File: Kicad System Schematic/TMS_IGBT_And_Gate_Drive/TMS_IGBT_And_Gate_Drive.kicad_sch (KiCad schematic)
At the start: 45 parts, among them J1 AFBR-1624Z, J2 AFBR-1624Z, J3 AFBR-2624Z, J4 AFBR-2624Z, J5 AFBR-2624Z, J6 AFBR-1624Z, J7 AFBR-2624Z, J8 AFBR-1624Z, Q1 FZ1200R33KF2, Q2 FZ1200R33KF2, T1 Microwave-Oven Transformer, T2 Microwave-Oven Transformer, T3 Variable Transformer, U1 Isolated DC-DC Converter, U2 Non-Isolated DC-DC Converter, U5 1SD418F2-FZ1200R33KF2, U6 1SD418F2-FZ1200R33KF2, U7 74HCT125N, U8 Non-Isolated DC-DC Converter

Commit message: updated schematic with some untested charge-controller circuitry. This is something I plan on building and testing.
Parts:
- added C17, C18, C22, C24: 100n, symbol Device:C
- added C19, C20, C21, C23, C27, C29, C33: 10u, symbol Device:C
- added C25, C30, C32: 1u, symbol Device:C
- added C26, C31: 0.1u, symbol Device:C
- added C28: 10000p, symbol Device:C
- added R1, R2: 4k7, symbol Device:R
- added R10, R11, R6, R9: 0, symbol Device:R
- added R12, R13, R14, R3, R4, R5: 5k1, symbol Device:R
- added R15, R16, R17, R18, R19, R20, R21, R22: 1M, Resistor_SMD:R_2512_6332Metric_Pad1.40x3.35mm_HandSolder, symbol Device:R
- added R7, R8: 10K, Resistor_SMD:R_1206_3216Metric_Pad1.30x1.75mm_HandSolder, symbol Device:R
- added U11: LM2931-5.0_SO8, Package_SO:SOIC-8_3.9x4.9mm_P1.27mm, symbol Regulator_Linear:LM2931-5.0_SO8
- added U12: ADS1115IDGS, Package_SO:TSSOP-10_3x3mm_P0.5mm, symbol Analog_ADC:ADS1115IDGS
- added U3: LM393, symbol Comparator:LM393
- added U4: AD5693RxRM, Package_SO:MSOP-10_3x3mm_P0.5mm, symbol Analog_DAC:AD5693RxRM
- added U9: Non-Isolated DC-DC Converter, Converter_DCDC:Converter_DCDC_Murata_OKI-78SR_Horizontal, symbol Converter_DCDC:OKI-78SR-5_1.5-W36H-C
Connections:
- net +24V: now also U9.1 (IN)
- net +3V3: now also C32.2, C33.2, U4.2 (VLOGIC)
- net +5V: now also C17.1, C18.1, C19.1, C20.1, C21.1, C22.1, C23.1, C24.1
- net GND: now also C1.2, C10.2, C11.2, C12.2, C13.2, C14.2, C15.2, C16.2, C2.2, D2.2 (A), D5.2 (A), D6.2 (A), MES2.2 (-), Q2.4 (Emitter_phase_1), Q2.6 (Emitter_phase_2), Q2.8 (Emitter_phase_3), C17.2, C18.2, C19.2, C20.2, C21.2, C22.2, C23.2, C24.2, C25.2, C26.2, C27.2, C28.2, C29.2, C30.2, C31.2, C32.1, C33.1, R1.1, R11.2, R2.1, R7.1, R8.1, R9.2, U11.2 (GND), U11.3 (GND), U11.6 (GND), U11.7 (GND), U12.3 (GND), U12.5 (AIN1), U12.6 (AIN2), U12.7 (AIN3), U12.8 (VDD), U4.4 (~{LDAC}), U4.5 (GND), U9.2 (GND)
- net at C1.1, C2.1, C3.1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: now also R15.2, R22.2
- new net: J1.4 (Fiber_Out), J2.4 (Fiber_Out), R1.2, R2.2, U7.3 (1Y)
- new net: R10.2, R11.1, U12.1 (ADDR)
- new net: R15.1, R16.2
- new net: R5.2, U4.3 (~{RESET})
- new net: R17.1, R18.2
- new net: R16.1, R17.2
- new net: R19.2, R20.1
- new net: R20.2, R21.1
- new net: R19.1, R7.2, U3.3 (+)
- new net: C28.1, U4.9 (VREF)
- new net: R18.1, R8.2, U12.4 (AIN0)
- new net: R21.2, R22.1
- new net: U3.2 (-), U4.10 (VOUT)
- new net: R6.2, R9.1, U4.6 (A0)
- new net +5V_LDO: C25.1, C26.1, C27.1, C29.1, C30.1, C31.1, R10.1, R12.1, R13.1, R14.1, R3.1, R4.1, R5.1, R6.1, U11.1 (OUT), U4.1 (VDD)
- new net +8V: U11.8 (IN), U9.3 (OUT)
- new net ADC_INT: R12.2, U12.2 (ALERT/RDY)
- new net ADC_SCL: R13.2, U12.10 (SCL)
- new net ADC_SDA: R14.2, U12.9 (SDA)
- new net DAC_SCL: R3.2, U4.7 (SCL)
- new net DAC_SDA: R4.2, U4.8 (SDA)
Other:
- note added: "COMPARATOR"
- note added: "DAC"
- note added: "HV Voltage Divider 1"
- note added: "HV Voltage Divider 2"

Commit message: updated schematic. Tried using DAC and comparator, it's too noisey, can't use opamps to filter noise. Instead using dedicated teensy to read ADC, do digital filtering/averaging and control charge circuit
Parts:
- added C34: 4u7, symbol Device:C
- added C35, C37: 1u, symbol Device:C
- added C36, C38, C39, C40: 10u, symbol Device:C
- added Q3: IRG4PF50W, Package_TO_SOT_THT:TO-247-3_Vertical, symbol Transistor_IGBT:IRG4PF50W
- added R23: 10, symbol Device:R
- added U10: MCP1415, Package_TO_SOT_SMD:SOT-23-5, symbol Driver_FET:MCP1415
- added U13: Isolated DC-DC Converter, Converter_DCDC:Converter_DCDC_Artesyn_ATA_SMD, symbol Converter_DCDC_Isolated:ATA00A36S-L
- added U14: ISO1644DWR, Package_SO:SOIC-16W_7.5x10.3mm_P1.27mm, symbol Isolator:ISO1644DWR
- added U15: LM2931-5.0_SO8, Package_SO:SOIC-8_3.9x4.9mm_P1.27mm, symbol Regulator_Linear:LM2931-5.0_SO8
- added U16: ADS8699IPWR, symbol Analog_ADC:ADS8699IPWR
- C28: footprint (none) -> Capacitor_SMD:C_0603_1608Metric
- U4: footprint Package_SO:MSOP-10_3x3mm_P0.5mm -> AD5683RARMZ:AD5683RARMZ
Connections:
- net +24V: now also U13.16 (+VIN)
- net +3V3: now also C40.1, U14.1 (VCC1)
- net DAC_SCL: now also A1.19 (I2C_0_SCL)
- net DAC_SDA: now also A1.18 (I2C_0_SDA)
- net GND: now also C40.2, Q3.2 (C), U13.1 (-VIN), U14.2 (GND1), U14.8 (GND1); no longer D5.2 (A), D6.2 (A), R8.1
- net ISO_+15V: now also U10.2 (Vdd)
- net ISO_GND: now also R8.1, C34.2, C35.2, C36.2, C37.2, C38.2, C39.2, U10.4 (GND), U13.10 (-VOUT), U14.15 (GND2), U14.9 (GND2), U15.2 (GND), U15.3 (GND), U15.6 (GND), U15.7 (GND), U16.1 (AGND), U16.15 (DGND), U16.3 (REFGND), U16.6 (AIN_GND)
- net at R18.1, R8.2, U12.4 (AIN0): now also U16.5 (AIN_P)
- net Charge_Switch: now reaches U3.1
- net Charge_Switch: now also U10.3 (IN)
- new net: U14.10 (INC), U16.11 (SDO-0)
- new net: U14.11 (SCL2), U16.7 (~{RST})
- new net: U14.12 (OUTB), U16.8 (SDI)
- new net: U14.13 (OUTA), U16.10 (SCLK)
- new net: U14.14 (SDA2), U16.9 (CONVST/~{CS})
- new net: Q3.1 (G), R23.1
- new net: D5.2 (A), D6.2 (A), Q3.3 (E)
- new net: C35.1, C36.1, U16.4 (REFCAP)
- new net: C34.1, U16.2 (REFIO)
- new net: R23.2, U10.5 (~{OUT})
- new net ISO_+5V_LDO: C37.1, C38.1, C39.1, U14.16 (VCC2), U15.1 (OUT), U16.14 (DVDD), U16.16 (AVDD)
- new net ISO_+8V: U13.9 (+VOUT), U15.8 (IN)
- new net ISO_ADC_CS/CONVST: A1.10 (SPI_0_CS), U14.3 (SDA1)
- new net ISO_ADC_RST: A1.9 (Digital_Out), U14.6 (SCL1)
- new net ISO_ADC_SCLK: A1.13 (SPI_0_SCK), U14.4 (INA)
- new net ISO_ADC_SDI: A1.11 (SPI_0_MOSI), U14.7 (OUT)
- new net ISO_ADC_SDO: A1.12 (SPI_0_MISO), U14.5 (INB)
- no-connect marks 7 -> 8
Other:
- note added: "PROBABLY NOT GOING TO USE DAC AND COMPARATOR. Can't find a way to filter noise in divided voltage. easier to filter/average digitally in teensy."
- note added: "PROBABLY NOT GOING TO USE THIS ADC. Using the ADS8699IPWR instead for higher sample rate"
- note added: "To Teensy"
- moved on the sheet: C25, C26, C27, C28, C29, C30, C31, C32, C33, D1, D4, D5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

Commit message: started updating schematic, need to find better symbol for the high voltage differential probes... Added first-draft of Bill-Of-Materials, just got the main power components for now. Will next add all components for the charge-controller and pulse-driver. Still need to upgrade pulse-driver to handle different protocols & patterns and have a single-shot mode. Right now I'm excited about finally building a system to measure/characterize and map the magnetic field strength of various coils I made compared to the one commercial coil I have. Can then compare these results to the simulations.
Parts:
- removed C39, C40: 10u, symbol Device:C
- removed R15, R16, R17, R18, R19, R20, R21, R22: 1M, Resistor_SMD:R_2512_6332Metric_Pad1.40x3.35mm_HandSolder, symbol Device:R
- removed R7, R8: 10K, Resistor_SMD:R_1206_3216Metric_Pad1.30x1.75mm_HandSolder, symbol Device:R
- removed U13: Isolated DC-DC Converter, Converter_DCDC:Converter_DCDC_Artesyn_ATA_SMD, symbol Converter_DCDC_Isolated:ATA00A36S-L
- removed U14: ISO1644DWR, Package_SO:SOIC-16W_7.5x10.3mm_P1.27mm, symbol Isolator:ISO1644DWR
- removed U15: LM2931-5.0_SO8, Package_SO:SOIC-8_3.9x4.9mm_P1.27mm, symbol Regulator_Linear:LM2931-5.0_SO8
- added MES4: HV Differential Probe, symbol Simulation_SPICE:VOLTMETER_DIFF
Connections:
- net ISO_+5V_LDO is gone; now on net +5V_LDO: C37.1, C38.1, U16.14 (DVDD), U16.16 (AVDD)
- net ISO_ADC_CS/CONVST is gone; now on net ADC_CS/CONVST: A1.10 (SPI_0_CS)
- net ISO_ADC_RST is gone; now on net ADC_RST: A1.9 (Digital_Out)
- net ISO_ADC_SCLK is gone; now on net ADC_SCLK: A1.13 (SPI_0_SCK)
- net ISO_ADC_SDI is gone; now on net ADC_SDI: A1.11 (SPI_0_MOSI)
- net ISO_ADC_SDO is gone; now on net ADC_SDO: A1.12 (SPI_0_MISO)
- net GND: now also C34.2, C35.2, C36.2, C37.2, C38.2, U16.1 (AGND), U16.15 (DGND), U16.3 (REFGND), U16.6 (AIN_GND), MES4.2 (-)
- net ISO_GND: no longer C34.2, C35.2, C36.2, C37.2, C38.2, U16.1 (AGND), U16.15 (DGND), U16.3 (REFGND), U16.6 (AIN_GND)
- net at C1.1, C2.1, C3.1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: now also MES4.1 (+)
- net ADC_SDO: now reaches U16.11 (SDO-0)
- net ADC_RST: now reaches U16.7 (~{RST})
- net ADC_SDI: now reaches U16.8 (SDI)
- net ADC_SCLK: now reaches U16.10 (SCLK)
- net ADC_CS/CONVST: now reaches U16.9 (CONVST/~{CS})
- net at U3.3 (+): now also U12.4 (AIN0), U16.5 (AIN_P), MES4.3 (out)
- net ADC_RVS: now reaches U16.13 (RVS)
- net ADC_RVS: now also A1.6 (Digital_In)
- net +8V renamed +7V5
- no-connect marks 8 -> 7
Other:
- note added: "Keeping this slow speed ADC to be able to verify the DAC output, and verify the high-speed ADC"
- note removed: "HV Voltage Divider 1"
- note removed: "HV Voltage Divider 2"
- note removed: "PROBABLY NOT GOING TO USE DAC AND COMPARATOR. Can't find a way to filter noise in divided voltage. easier to filter/average digitally in teensy."
- note removed: "PROBABLY NOT GOING TO USE THIS ADC. Using the ADS8699IPWR instead for higher sample rate"
- moved on the sheet: C25, C26, C27, C28, C32, C33, R3, R4, R5, R6, R9, U3A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

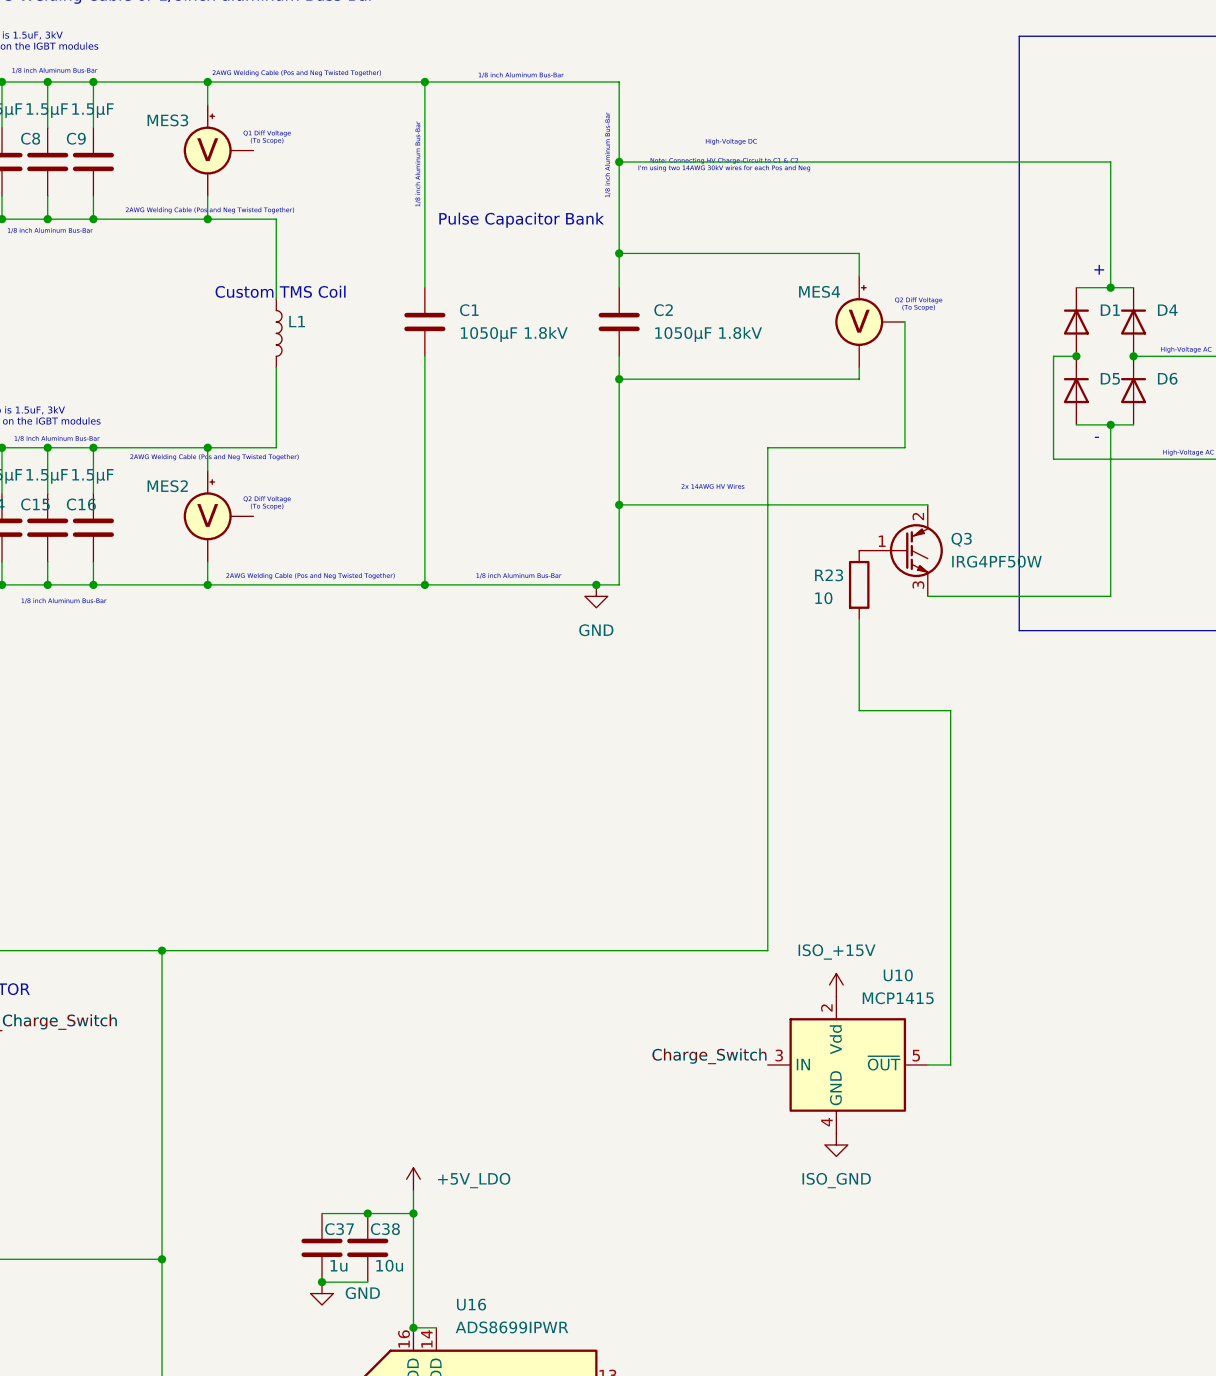
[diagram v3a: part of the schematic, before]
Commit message: added datasheets for Micsig high-voltage differential probes, and updated schematic symbol for the probes. Saw something cool in the new micsig probes, where they have a serial interface and serial number; might use this to store specific calibrations for various probes....
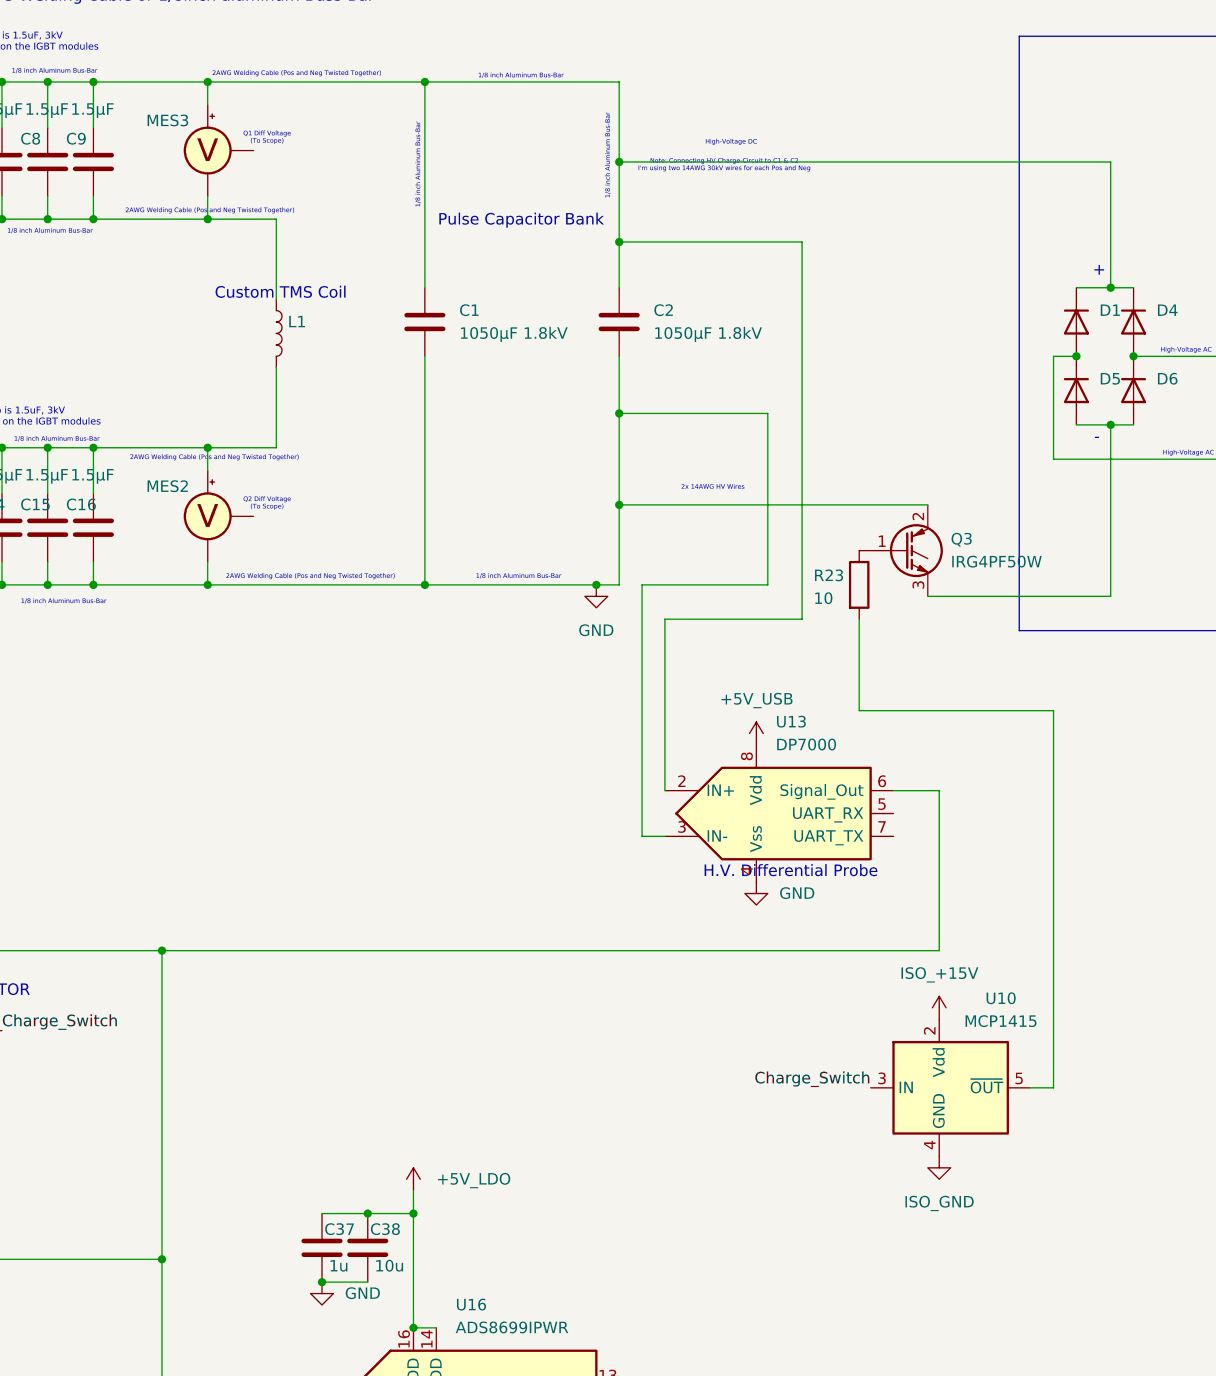
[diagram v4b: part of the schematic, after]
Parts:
- removed MES4: HV Differential Probe, symbol Simulation_SPICE:VOLTMETER_DIFF
- added U13: DP7000, symbol Analog_ADC:High-Voltage_Differential_Oscilliscope_Probe
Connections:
- net GND: now also U13.3 (IN-), U13.4 (Vss)
- net at C1.1, C2.1, C3.1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: now also U13.2 (IN+)
- net at U12.4 (AIN0), U16.5 (AIN_P), U3.3 (+): now also U13.6 (Signal_Out)
- new net +5V_USB: U13.8 (Vdd)
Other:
- note added: "H.V. Differential Probe"
- moved on the sheet: U10
